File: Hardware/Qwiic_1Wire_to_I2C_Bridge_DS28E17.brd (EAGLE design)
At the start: 45.7 x 27.9 mm, 23 parts, among them J1 RJ45, J2 RJ45, J3 RJ11, J4 RJ11, U1 DS28E17

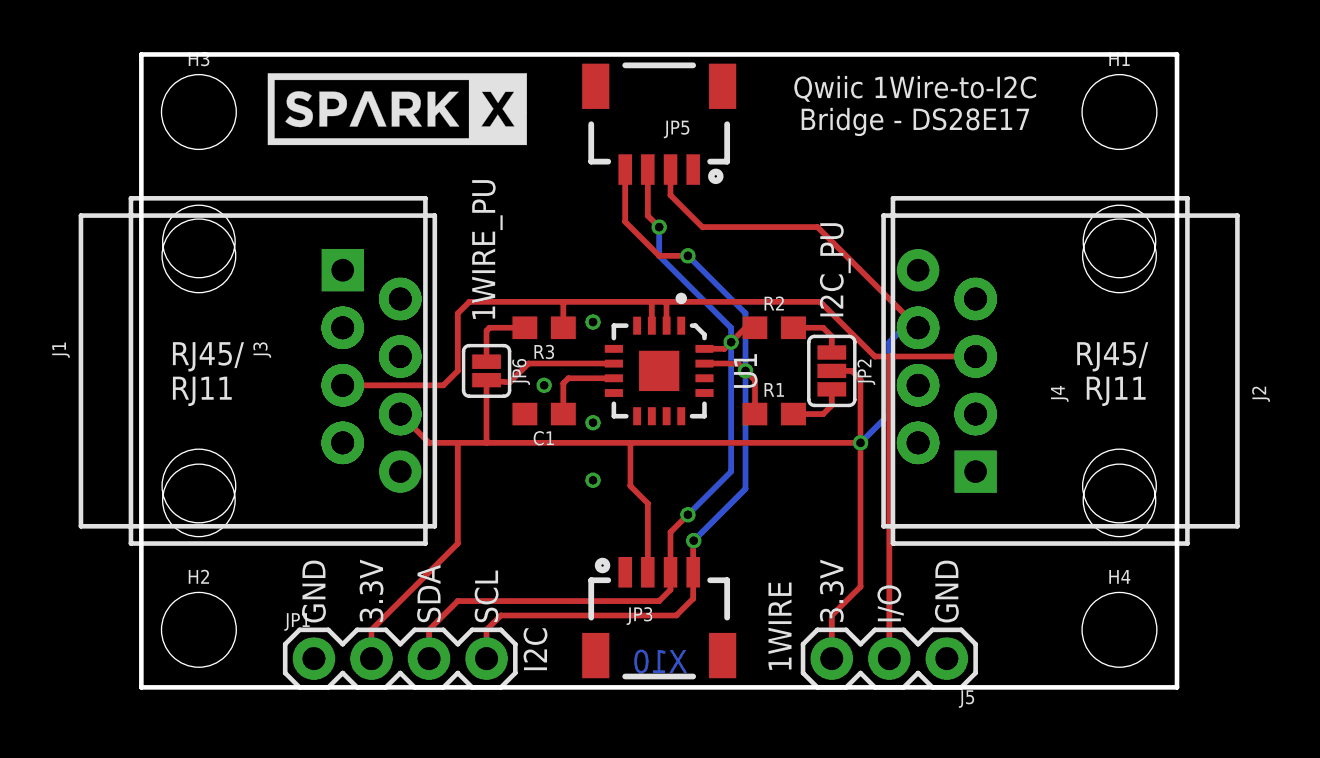
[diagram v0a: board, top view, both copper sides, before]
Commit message: Added RJ45/RJ11 footprint. CAM new panel gerbers
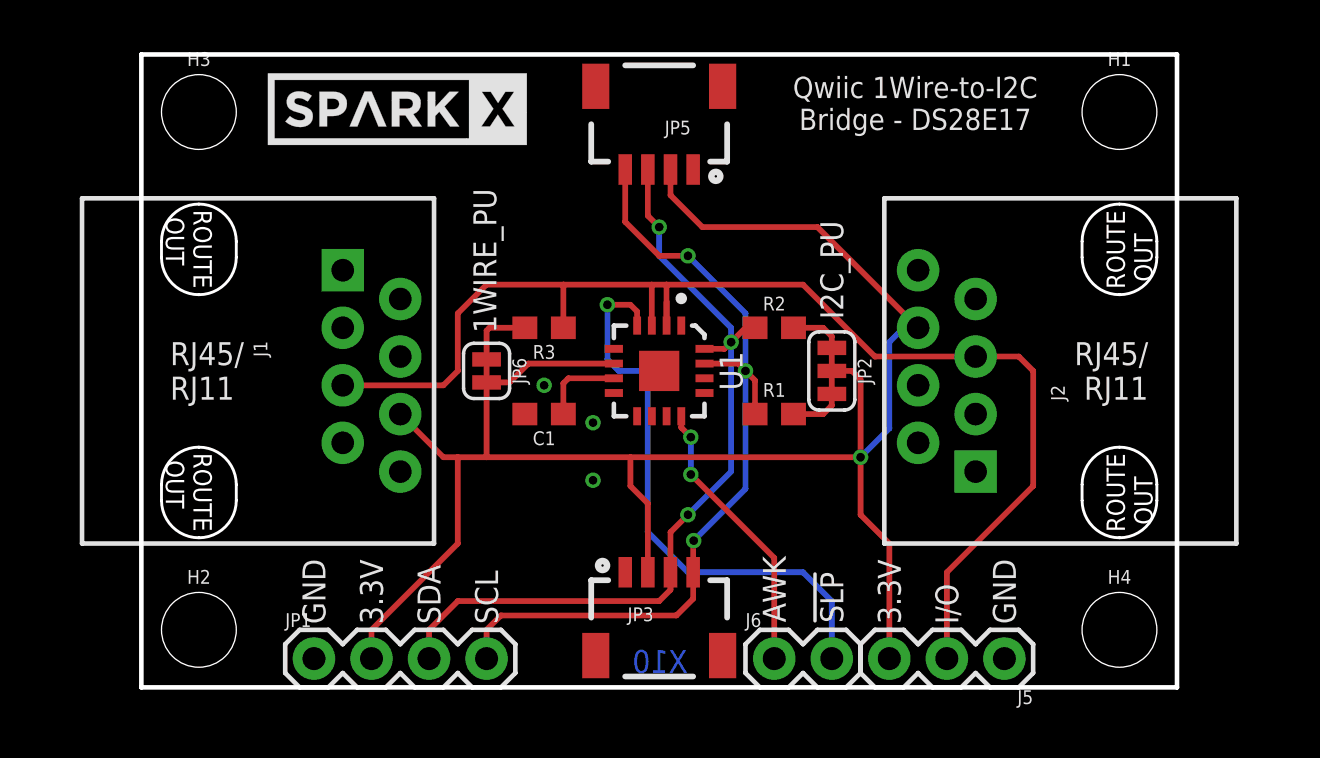
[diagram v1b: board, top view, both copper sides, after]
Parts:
- removed J3, J4: RJ11, SparkFun-Connectors:RJ11-6
- added J6: (no value), SparkFun-Connectors:1X02
- added JP4: (no value), SparkFun-Jumpers:SMT-JUMPER_2_NC_TRACE_SILK
- J1, J2: value RJ45 -> RJ45_RJ11_COMBO; device SparkFun-Connectors:RJ45-8 -> SparkX:RJ45_RJ11_COMBO
- JP2: device SparkFun-Jumpers:SMT-JUMPER_3_2-NC_PASTE_SILK -> SparkFun-Jumpers:SMT-JUMPER_3_2-NC_TRACE_SILK
- JP6: device SparkFun-Jumpers:SMT-JUMPER_2_NC_PASTE_SILK -> SparkFun-Jumpers:SMT-JUMPER_2_NC_TRACE_SILK
- moved LOGO1 10.2 mm to (22.9, 3.81)
- moved J5 2.54 mm to (38.1, 1.27)
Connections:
- new net !SLEEP: J6.2, JP4.1, U1.4
- net 3.3V: no longer J3.5, J4.5
- net AWAKE: now also J6.1
- net GND: now also JP4.2; no longer J3.3, J4.3, U1.4
- net IO: no longer J3.4, J4.4
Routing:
- net !SLEEP: track 0.00 -> 25.5 mm, vias 0 -> 1
- net AWAKE: track 0.00 -> 12.4 mm, vias 0 -> 2
- net IO: track 48.5 -> 56.2 mm
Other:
- board text added: "!SLP"
- board text added: "AWK"
- board text added: "SLEEP"
